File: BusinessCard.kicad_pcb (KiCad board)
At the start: 2 copper layers, 100 x 50 mm, 121 parts, among them J1 USB_C_Receptacle_USB2.0, SW1 SW_Push_45deg, SW10 SW_Push_45deg, SW11 SW_Push_45deg, SW12 SW_Push_45deg, SW13 SW_Push_45deg, SW14 SW_Push_45deg, SW15 SW_Push_45deg, SW16 SW_Push_45deg, SW17 SW_Push_45deg, SW18 SW_Push_45deg, SW19 SW_Push_45deg, SW2 SW_Push_45deg, SW20 SW_Push_45deg, SW21 SW_Push_45deg, SW22 SW_Push_45deg, SW23 SW_Push_45deg, SW24 SW_Push_45deg, SW25 SW_Push_45deg, SW26 SW_Push_45deg, SW27 SW_Push_45deg, SW28 SW_Push_45deg, SW29 SW_Push_45deg, SW3 SW_Push_45deg, SW30 SW_Push_45deg, SW31 SW_Push_45deg, SW32 SW_Push_45deg, SW33 SW_Push_45deg, SW34 SW_Push_45deg, SW35 SW_Push_45deg, SW36 SW_Push_45deg, SW37 SW_Push_45deg, SW38 SW_Push_45deg, SW39 SW_Push_45deg, SW4 SW_Push_45deg, SW40 SW_Push_45deg, SW41 SW_Push_45deg, SW42 SW_Push_45deg, SW43 SW_Push_45deg, SW44 SW_Push_45deg, SW45 SW_Push_45deg, SW46 SW_Push_45deg, SW47 SW_Push_45deg, SW48 SW_Push_45deg, SW5 SW_Push_45deg, SW6 SW_Push_45deg, SW7 SW_Push_45deg, SW8 SW_Push_45deg, SW9 SW_Push_45deg, U1 STM32F103C8Tx, U2 XC6206PxxxMR, U3 SRV05-4, Y1 8MHz

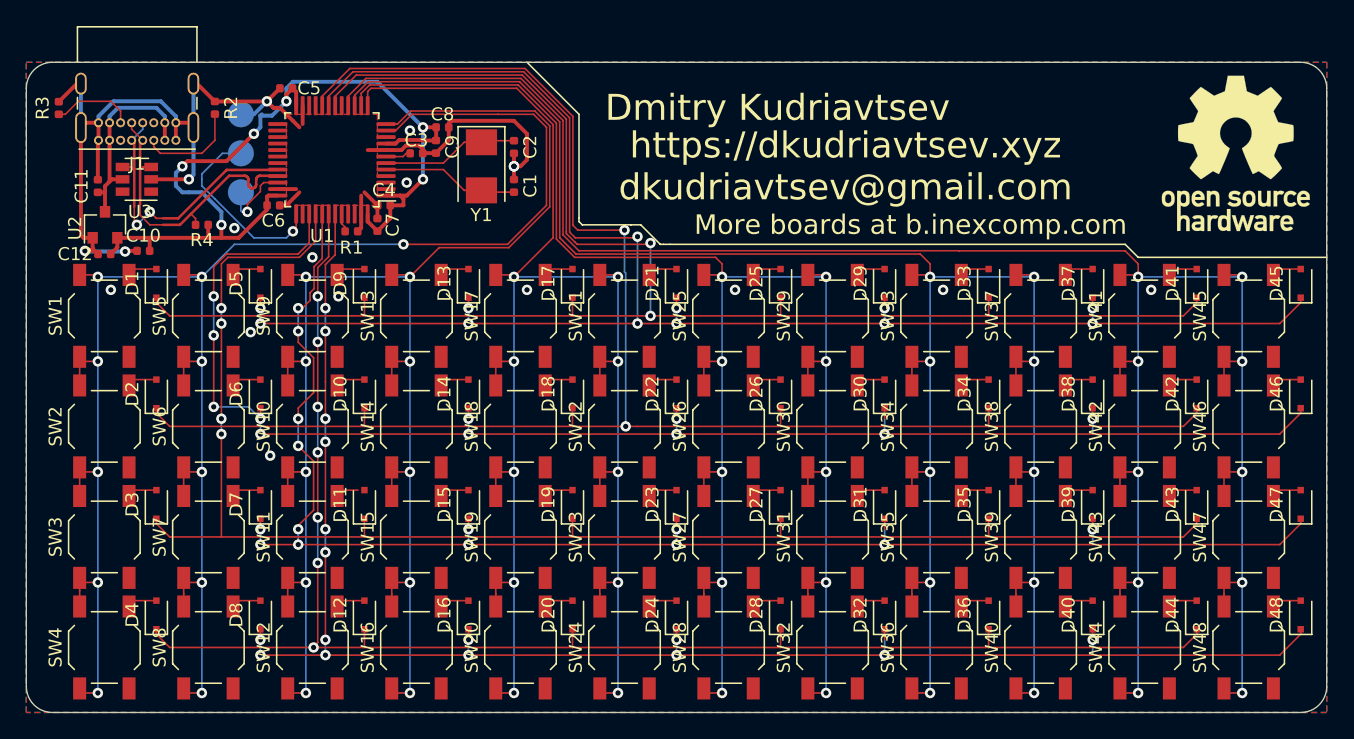
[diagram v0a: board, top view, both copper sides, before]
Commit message: Added proper silkscreen for keys
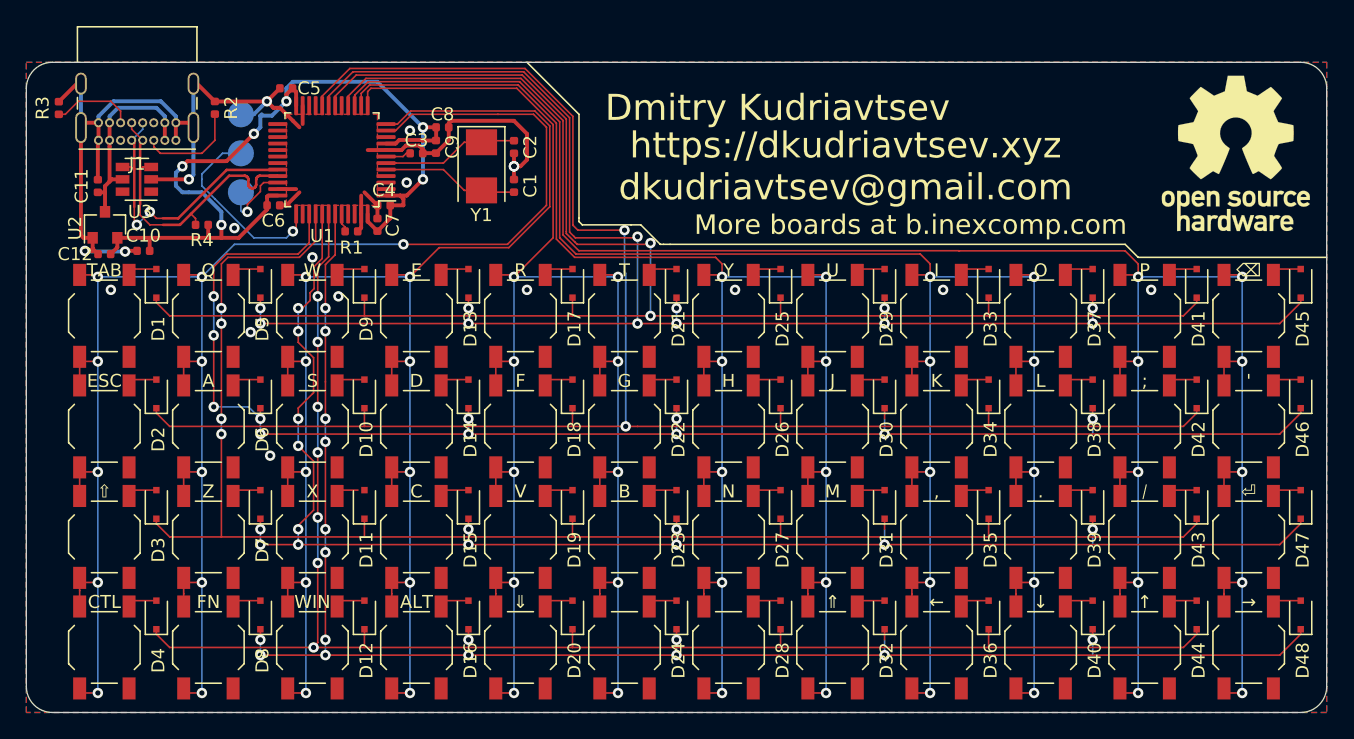
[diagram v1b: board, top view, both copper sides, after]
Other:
- board text added: "'"
- board text added: ","
- board text added: "."
- board text added: "/"
- board text added: ";"
- board text added: "A"
- board text added: "ALT"
- board text added: "B"
- board text added: "C"
- board text added: "CTL"
- board text added: "D"
- board text added: "E"
- board text added: "ESC"
- board text added: "F"
- board text added: "FN"
- board text added: "G"
- board text added: "H"
- board text added: "I"
- board text added: "J"
- board text added: "K"
- board text added: "L"
- board text added: "M"
- board text added: "N"
- board text added: "O"
- board text added: "P"
- board text added: "Q"
- board text added: "R"
- board text added: "S"
- board text added: "T"
- board text added: "TAB"
- board text added: "U"
- board text added: "V"
- board text added: "W"
- board text added: "WIN"
- board text added: "X"
- board text added: "Y"
- board text added: "Z"
- board text added: "←"
- board text added: "↑"
- board text added: "→"
- board text added: "↓"
- board text added: "⇑"
- board text added: "⇓"
- board text added: "⇧"
- board text added: "⌫"
- board text added: "⏎"

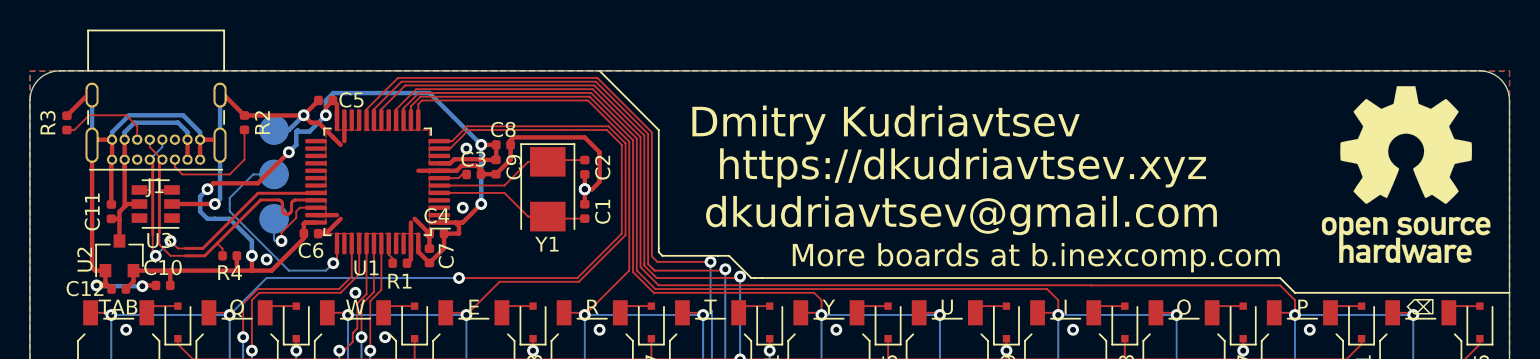
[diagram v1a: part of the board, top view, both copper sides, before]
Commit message: Floated the shield
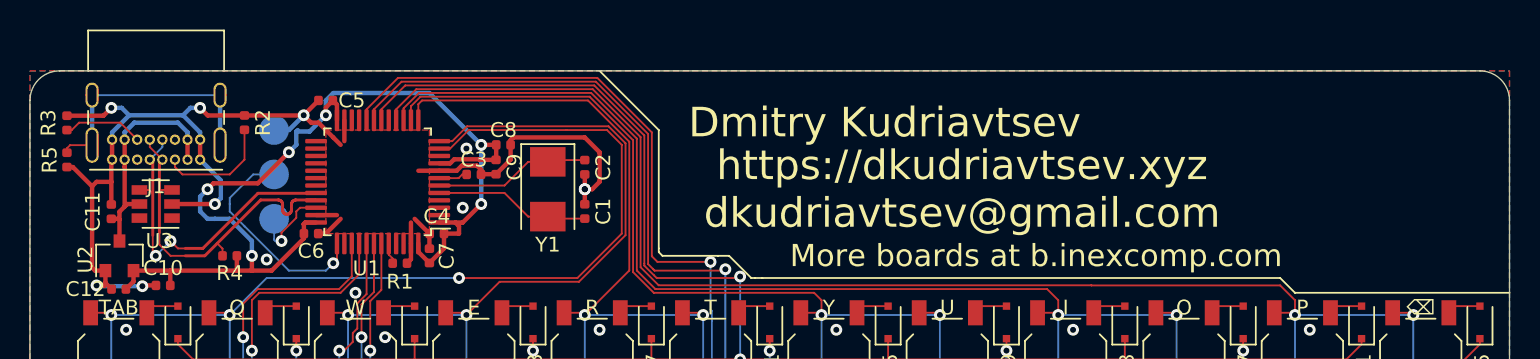
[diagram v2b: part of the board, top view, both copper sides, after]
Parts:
- removed REF**: OSHW-Logo_11.4x12mm_SilkScreen, Symbol:OSHW-Logo_11.4x12mm_SilkScreen
- added R5: 1M, Resistor_SMD:R_0402_1005Metric, F.Cu at (52.5, 56.0)
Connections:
- J1 pad S1: GND -> Net-(J1-PadS1)
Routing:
- net Net-(J1-PadS1): track 0.00 -> 18.1 mm
- net GND: track 91.9 -> 87.4 mm, vias 18 -> 20
- net /MCU Support/CC2: track 6.37 -> 5.43 mm

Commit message: Fixed bad routing
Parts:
- moved C4 1.58 mm to (79.0, 61.5)
- moved C6 1.00 mm to (69.0, 62.0)
- moved C5 0.50 mm to (70.0, 51.5)
- moved C7 0.50 mm to (77.5, 62.5)
- moved R1 0.50 mm to (75.0, 63.5)
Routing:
- net VBAT: track 71.6 -> 73.9 mm
- net GND: track 87.4 -> 88.2 mm, vias 20 -> 24
- net Net-(D9-Pad2): track 2.29 -> 1.65 mm
- net Net-(D11-Pad2): track 1.65 -> 2.15 mm
- net BOOT0: track 1.45 -> 1.95 mm
- net row7: vias 16 -> 18
- net row3: vias 11 -> 13
- net row5: vias 14 -> 16

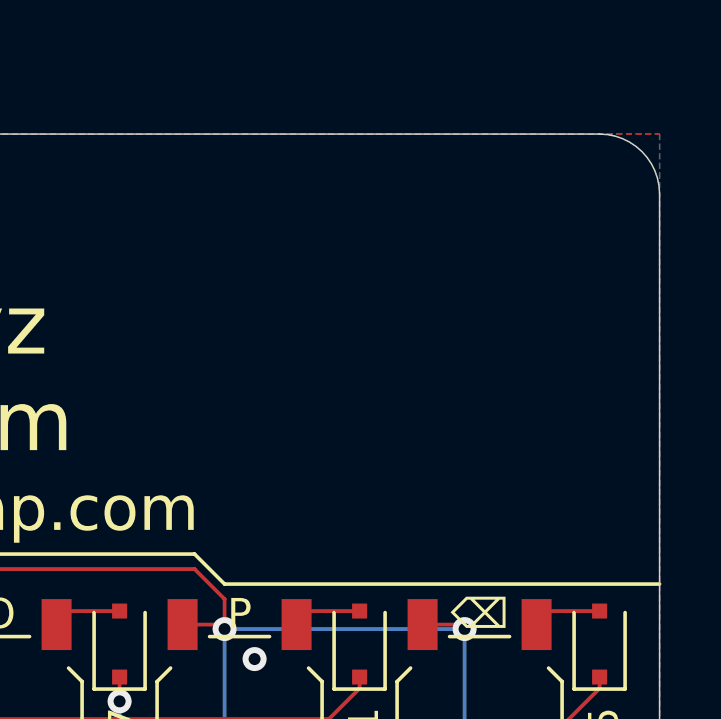
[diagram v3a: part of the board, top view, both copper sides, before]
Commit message: fixed footprint
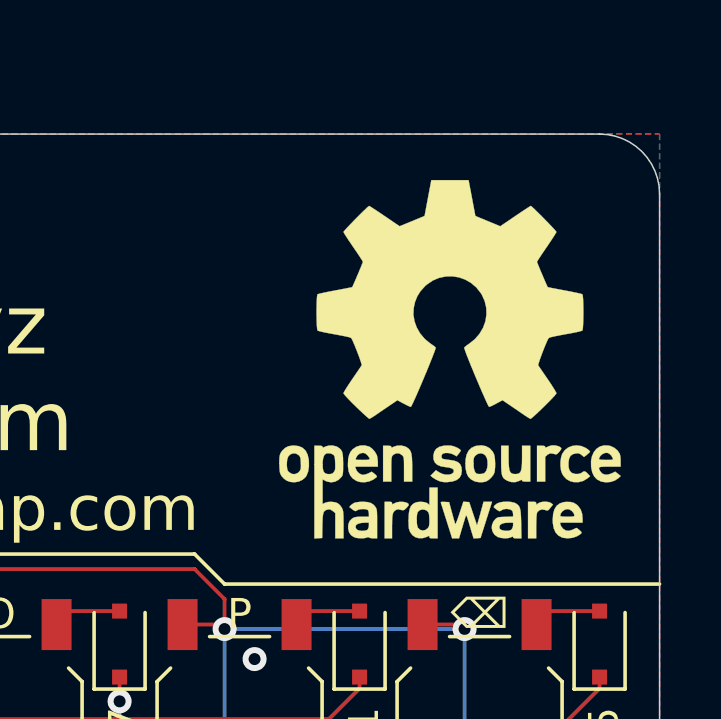
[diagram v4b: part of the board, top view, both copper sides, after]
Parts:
- added REF**: OSHW-Logo_11.4x12mm_SilkScreen, Symbol:OSHW-Logo_11.4x12mm_SilkScreen, F.Cu at (143.0, 57.5)
